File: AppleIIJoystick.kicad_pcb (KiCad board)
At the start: 2 copper layers, 18 parts, among them J1 DB9_Male, J2 Parallax_27800_Joystick, SW1 SW_Push, SW2 SW_Push

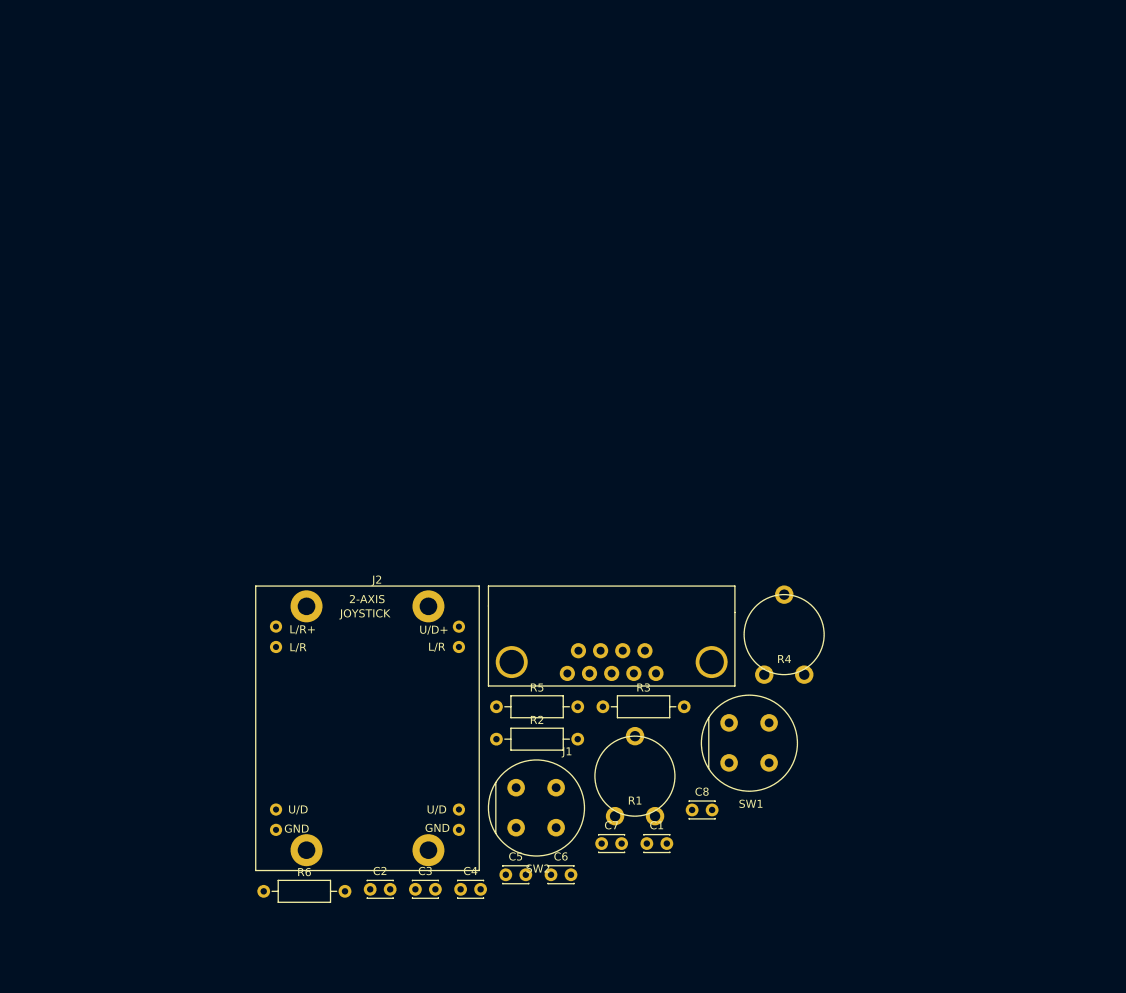
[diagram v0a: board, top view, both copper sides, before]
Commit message: swapped out buttons. new footprint/3d model.
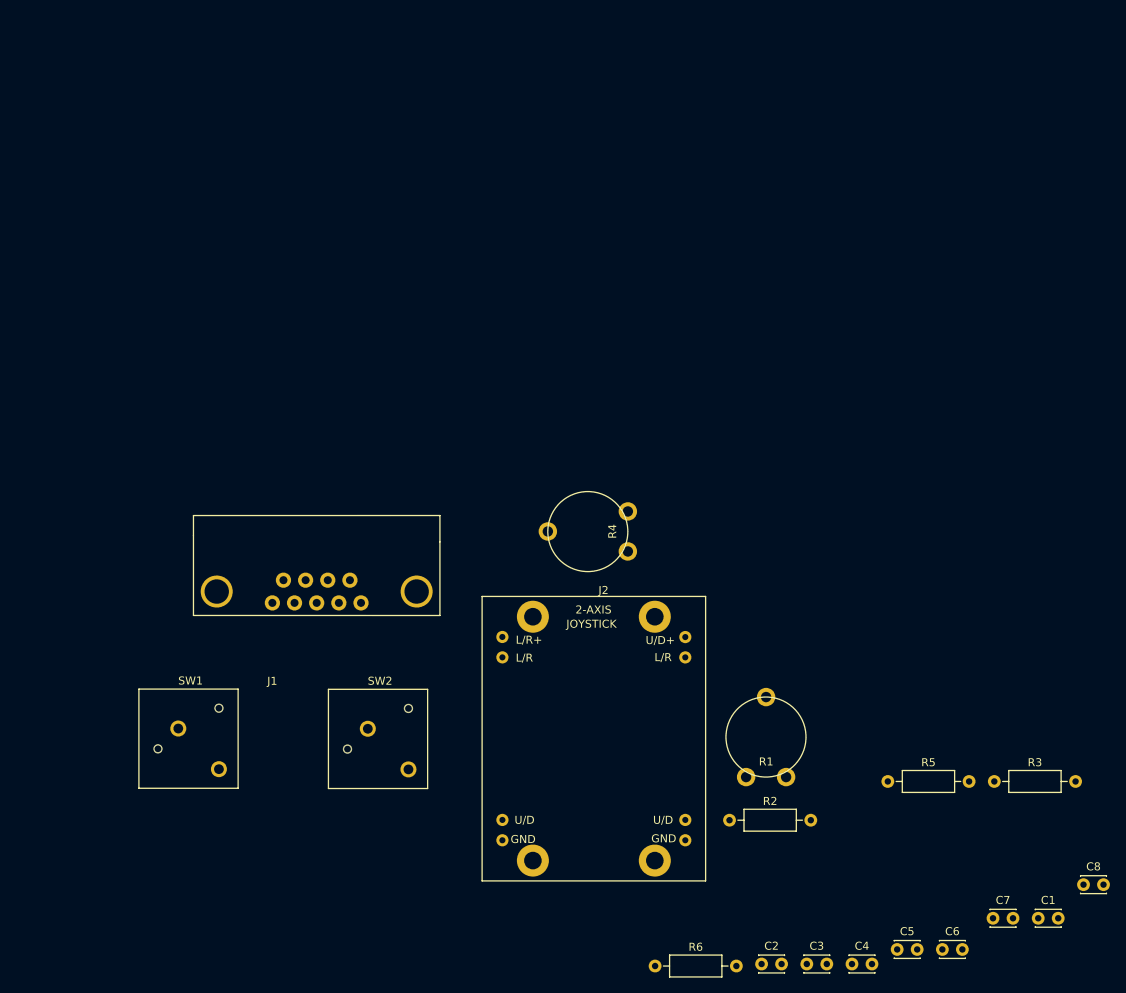
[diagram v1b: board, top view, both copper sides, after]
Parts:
- SW1, SW2: footprint AppleIIJoystick:D6C_BUTTON -> AppleIIJoystick:ESWITCH_E11GRY_BTN
- moved SW1 64.0 mm to (100.8, 134.1)
- moved C1 49.8 mm to (203.2, 152.8)
- moved C4 49.8 mm to (180.0, 158.5)
- moved C5 49.8 mm to (185.6, 156.7)
- moved C7 49.8 mm to (197.6, 152.8)
- moved C8 49.8 mm to (208.9, 148.6)
- moved R3 49.8 mm to (197.8, 135.7)
- moved C2 49.8 mm to (168.7, 158.5)
- moved C3 49.8 mm to (174.3, 158.5)
- moved R6 49.8 mm to (155.4, 158.7)
- moved C6 49.8 mm to (191.3, 156.7)
- moved R5 49.8 mm to (184.4, 135.7)
- moved J1 37.9 mm to (107.5, 113.3)
- moved R2 30.8 mm to (164.7, 140.5)
- moved R4 30.6 mm to (142.0, 104.4), turned to 90 degrees
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
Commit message: adding edge cuts layer and board outline
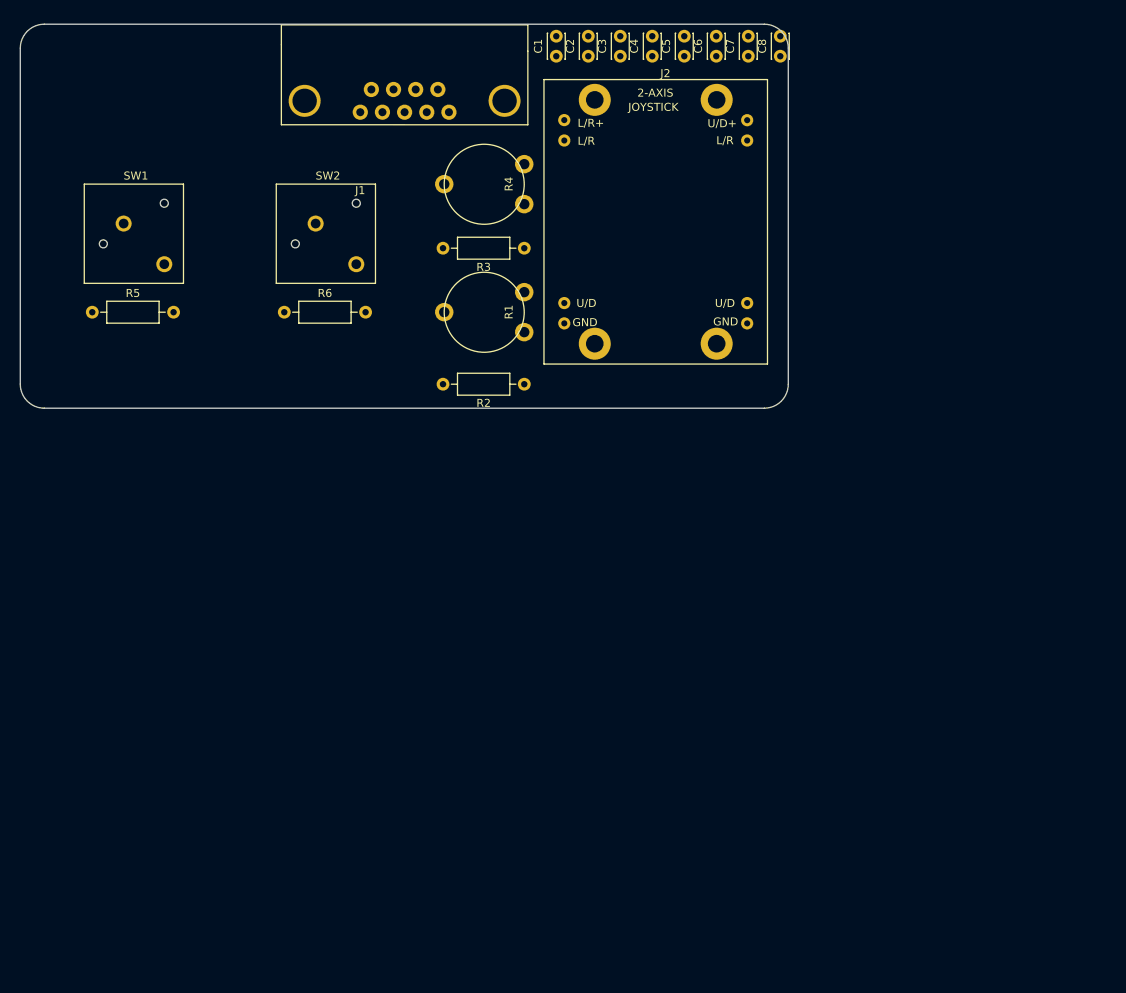
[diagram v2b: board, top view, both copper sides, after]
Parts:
- moved C1 123.5 mm to (143.0, 45.0), turned to 90 degrees
- moved C4 116.2 mm to (155.0, 45.0), turned to 90 degrees
- moved C3 115.8 mm to (151.0, 45.0), turned to 90 degrees
- moved C2 115.5 mm to (147.0, 45.0), turned to 90 degrees
- moved R5 115.5 mm to (85.0, 77.0)
- moved C6 115.2 mm to (163.0, 45.0), turned to 90 degrees
- moved C5 114.8 mm to (159.0, 45.0), turned to 90 degrees
- moved C7 112.0 mm to (167.0, 45.0), turned to 90 degrees
- moved C8 110.3 mm to (171.0, 45.0), turned to 90 degrees
- moved R6 94.0 mm to (109.0, 77.0)
- moved R3 88.9 mm to (139.0, 69.0), turned to 180 degrees
- moved J2 65.1 mm to (144.0, 53.0)
- moved SW1 63.5 mm to (94.0, 71.0)
- moved SW2 63.5 mm to (118.0, 71.0)
- moved R1 62.7 mm to (129.0, 77.0), turned to 90 degrees
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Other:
- board outline added: 96 x 48 mm

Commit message: board layout
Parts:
- moved C4 4.12 mm to (150.9, 44.8)
- moved C8 3.52 mm to (167.5, 44.9)
- moved C3 2.76 mm to (148.2, 44.8)
- moved C7 2.16 mm to (164.8, 44.9)
- moved C2 1.41 mm to (145.6, 44.8)
- moved C6 0.81 mm to (162.2, 44.9)
- moved C5 0.57 mm to (159.6, 44.9)
- moved C1 0.20 mm to (143.0, 44.8)
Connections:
- R1 pad 1: Net-(R1-Pad1) -> /LR
- R1 pad 2: /LR -> Net-(R1-Pad2)
- R2 pad 2: Net-(R1-Pad1) -> Net-(R1-Pad2)
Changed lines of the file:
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@@
   (net 12 "Net-(J2-Pad8)")
   (net 13 "Net-(J2-Pad1)")
-  (net 14 "Net-(R1-Pad1)")
-  (net 15 "Net-(R3-Pad2)")
+  (net 14 "Net-(R3-Pad2)")
+  (net 15 "Net-(R1-Pad2)")
   (net_class Default "This is the default net class."
     (clearance 0.2)
@@
     (add_net "Net-(J2-Pad5)")
     (add_net "Net-(J2-Pad8)")
-    (add_net "Net-(R1-Pad1)")
+    (add_net "Net-(R1-Pad2)")
     (add_net "Net-(R3-Pad2)")
   )
   (module Capacitor_THT:C_Disc_D3.0mm_W2.0mm_P2.50mm (layer F.Cu)
-    (at 143 45 90)
-    (descr "C, Disc series, Radial, pin pitch=2.50mm, , diameter*width=3*2mm^2, Capacitor")
-    (tags "C Disc series Radial pin pitch 2.50mm  diameter 3mm width 2mm Capacitor")
-    (fp_text reference C1 (at 1.25 -2.25 90) (layer F.SilkS)
+    (at 142.96644 44.8056 90)
+    (descr "C, Disc series, Radial, pin pitch=2.50mm, , diameter*width=3*2mm^2, Capacitor")
+    (tags "C Disc series Radial pin pitch 2.50mm  diameter 3mm width 2mm Capacitor")
+    (fp_text reference C1 (at -1.91634 0.03248 90) (layer F.SilkS)
       (effects (font (size 1 1) (thickness 0.15)))
     )
@@
   )
   (module Capacitor_THT:C_Disc_D3.0mm_W2.0mm_P2.50mm (layer F.Cu)
-    (at 147 45 90)
-    (descr "C, Disc series, Radial, pin pitch=2.50mm, , diameter*width=3*2mm^2, Capacitor")
-    (tags "C Disc series Radial pin pitch 2.50mm  diameter 3mm width 2mm Capacitor")
-    (fp_text reference C2 (at 1.25 -2.25 90) (layer F.SilkS)
+    (at 145.6055 44.8056 90)
+    (descr "C, Disc series, Radial, pin pitch=2.50mm, , diameter*width=3*2mm^2, Capacitor")
+    (tags "C Disc series Radial pin pitch 2.50mm  diameter 3mm width 2mm Capacitor")
+    (fp_text reference C2 (at -1.94936 0.0914 90) (layer F.SilkS)
       (effects (font (size 1 1) (thickness 0.15)))
     )
@@
   )
   (module Capacitor_THT:C_Disc_D3.0mm_W2.0mm_P2.50mm (layer F.Cu)
-    (at 151 45 90)
-    (descr "C, Disc series, Radial, pin pitch=2.50mm, , diameter*width=3*2mm^2, Capacitor")
-    (tags "C Disc series Radial pin pitch 2.50mm  diameter 3mm width 2mm Capacitor")
-    (fp_text reference C3 (at 1.25 -2.25 90) (layer F.SilkS)
+    (at 148.24456 44.8056 90)
+    (descr "C, Disc series, Radial, pin pitch=2.50mm, , diameter*width=3*2mm^2, Capacitor")
+    (tags "C Disc series Radial pin pitch 2.50mm  diameter 3mm width 2mm Capacitor")
+    (fp_text reference C3 (at -1.91634 0.04872 90) (layer F.SilkS)
       (effects (font (size 1 1) (thickness 0.15)))
     )
@@
   )
   (module Capacitor_THT:C_Disc_D3.0mm_W2.0mm_P2.50mm (layer F.Cu)
-    (at 155 45 90)
-    (descr "C, Disc series, Radial, pin pitch=2.50mm, , diameter*width=3*2mm^2, Capacitor")
-    (tags "C Disc series Radial pin pitch 2.50mm  diameter 3mm width 2mm Capacitor")
-    (fp_text reference C4 (at 1.25 -2.25 90) (layer F.SilkS)
+    (at 150.88362 44.8056 90)
+    (descr "C, Disc series, Radial, pin pitch=2.50mm, , diameter*width=3*2mm^2, Capacitor")
+    (tags "C Disc series Radial pin pitch 2.50mm  diameter 3mm width 2mm Capacitor")
+    (fp_text reference C4 (at -1.94936 0.00858 90) (layer F.SilkS)
       (effects (font (size 1 1) (thickness 0.15)))
     )
@@
   )
   (module Capacitor_THT:C_Disc_D3.0mm_W2.0mm_P2.50mm (layer F.Cu)
-    (at 159 45 90)
-    (descr "C, Disc series, Radial, pin pitch=2.50mm, , diameter*width=3*2mm^2, Capacitor")
-    (tags "C Disc series Radial pin pitch 2.50mm  diameter 3mm width 2mm Capacitor")
-    (fp_text reference C5 (at 1.25 -2.25 90) (layer F.SilkS)
+    (at 159.56134 44.90094 90)
+    (descr "C, Disc series, Radial, pin pitch=2.50mm, , diameter*width=3*2mm^2, Capacitor")
+    (tags "C Disc series Radial pin pitch 2.50mm  diameter 3mm width 2mm Capacitor")
+    (fp_text reference C5 (at -1.9519 -0.0341 90) (layer F.SilkS)
       (effects (font (size 1 1) (thickness 0.15)))
     )
@@
   )
   (module Capacitor_THT:C_Disc_D3.0mm_W2.0mm_P2.50mm (layer F.Cu)
-    (at 163 45 90)
-    (descr "C, Disc series, Radial, pin pitch=2.50mm, , diameter*width=3*2mm^2, Capacitor")
-    (tags "C Disc series Radial pin pitch 2.50mm  diameter 3mm width 2mm Capacitor")
-    (fp_text reference C6 (at 1.25 -2.25 90) (layer F.SilkS)
+    (at 162.19932 44.90466 90)
+    (descr "C, Disc series, Radial, pin pitch=2.50mm, , diameter*width=3*2mm^2, Capacitor")
+    (tags "C Disc series Radial pin pitch 2.50mm  diameter 3mm width 2mm Capacitor")
+    (fp_text reference C6 (at -1.9519 0.02482 90) (layer F.SilkS)
       (effects (font (size 1 1) (thickness 0.15)))
     )
@@
   )
   (module Capacitor_THT:C_Disc_D3.0mm_W2.0mm_P2.50mm (layer F.Cu)
-    (at 167 45 90)
-    (descr "C, Disc series, Radial, pin pitch=2.50mm, , diameter*width=3*2mm^2, Capacitor")
-    (tags "C Disc series Radial pin pitch 2.50mm  diameter 3mm width 2mm Capacitor")
-    (fp_text reference C7 (at 1.25 -2.25 90) (layer F.SilkS)
+    (at 164.83838 44.90466 90)
+    (descr "C, Disc series, Radial, pin pitch=2.50mm, , diameter*width=3*2mm^2, Capacitor")
+    (tags "C Disc series Radial pin pitch 2.50mm  diameter 3mm width 2mm Capacitor")
+    (fp_text reference C7 (at -1.9519 0.0812 90) (layer F.SilkS)
       (effects (font (size 1 1) (thickness 0.15)))
     )
@@
   )
   (module Capacitor_THT:C_Disc_D3.0mm_W2.0mm_P2.50mm (layer F.Cu)
-    (at 171 45 90)
-    (descr "C, Disc series, Radial, pin pitch=2.50mm, , diameter*width=3*2mm^2, Capacitor")
-    (tags "C Disc series Radial pin pitch 2.50mm  diameter 3mm width 2mm Capacitor")
-    (fp_text reference C8 (at 1.25 -2.25 90) (layer F.SilkS)
+    (at 167.47744 44.90466 90)
+    (descr "C, Disc series, Radial, pin pitch=2.50mm, , diameter*width=3*2mm^2, Capacitor")
+    (tags "C Disc series Radial pin pitch 2.50mm  diameter 3mm width 2mm Capacitor")
+    (fp_text reference C8 (at -1.9519 0.03852 90) (layer F.SilkS)
       (effects (font (size 1 1) (thickness 0.15)))
     )
@@
     (fp_circle (center -0.00762 4.9911) (end 0.01524 9.99236) (layer F.SilkS) (width 0.15))
     (pad 1 thru_hole circle (at 0.00762 -0.00508 90) (size 2.3 2.3) (drill 1.3) (layers *.Cu *.Mask)
-      (net 14 "Net-(R1-Pad1)"))
+      (net 1 /LR))
     (pad 2 thru_hole circle (at 2.50762 9.99492 90) (size 2.3 2.3) (drill 1.3) (layers *.Cu *.Mask)
-      (net 1 /LR))
+      (net 15 "Net-(R1-Pad2)"))
     (pad 3 thru_hole circle (at -2.49238 9.99492 90) (size 2.3 2.3) (drill 1.3) (layers *.Cu *.Mask))
     (model ${KIPRJMOD}/10-PIHER_3D_PT10LV10.STEP
@@
       (net 13 "Net-(J2-Pad1)"))
     (pad 2 thru_hole oval (at 10.16 0 180) (size 1.6 1.6) (drill 0.8) (layers *.Cu *.Mask)
-      (net 14 "Net-(R1-Pad1)"))
+      (net 15 "Net-(R1-Pad2)"))
     (model ${KISYS3DMOD}/Resistor_THT.3dshapes/R_Axial_DIN0207_L6.3mm_D2.5mm_P10.16mm_Horizontal.wrl
       (at (xyz 0 0 0))
@@
     (fp_line (start 1.93 -1.25) (end 1.93 1.25) (layer F.Fab) (width 0.1))
     (pad 2 thru_hole oval (at 10.16 0 180) (size 1.6 1.6) (drill 0.8) (layers *.Cu *.Mask)
-      (net 15 "Net-(R3-Pad2)"))
+      (net 14 "Net-(R3-Pad2)"))
     (pad 1 thru_hole circle (at 0 0 180) (size 1.6 1.6) (drill 0.8) (layers *.Cu *.Mask)
       (net 12 "Net-(J2-Pad8)"))
@@
     (pad 3 thru_hole circle (at -2.49238 9.99492 90) (size 2.3 2.3) (drill 1.3) (layers *.Cu *.Mask))
     (pad 2 thru_hole circle (at 2.50762 9.99492 90) (size 2.3 2.3) (drill 1.3) (layers *.Cu *.Mask)
-      (net 15 "Net-(R3-Pad2)"))
+      (net 14 "Net-(R3-Pad2)"))
     (pad 1 thru_hole circle (at 0.00762 -0.00508 90) (size 2.3 2.3) (drill 1.3) (layers *.Cu *.Mask)
       (net 3 /UD))

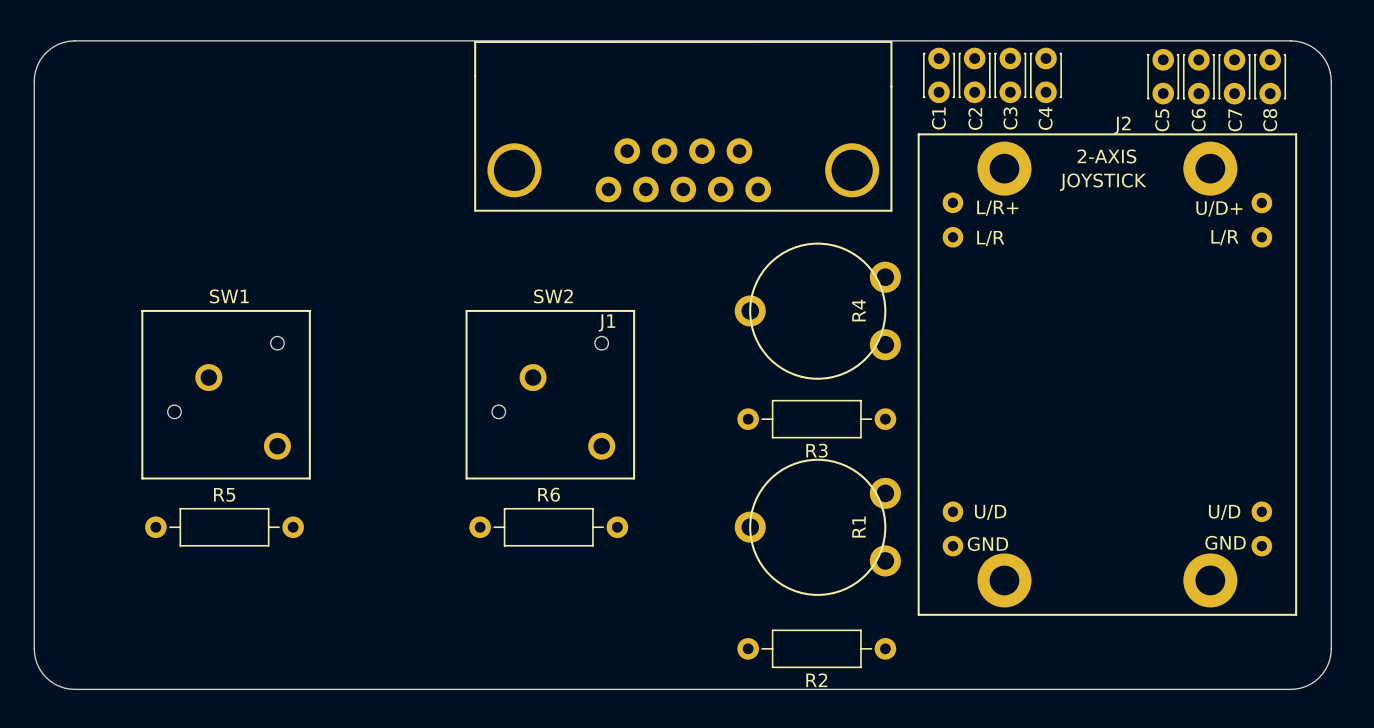
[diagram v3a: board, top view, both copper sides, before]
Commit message: finished routing pcb
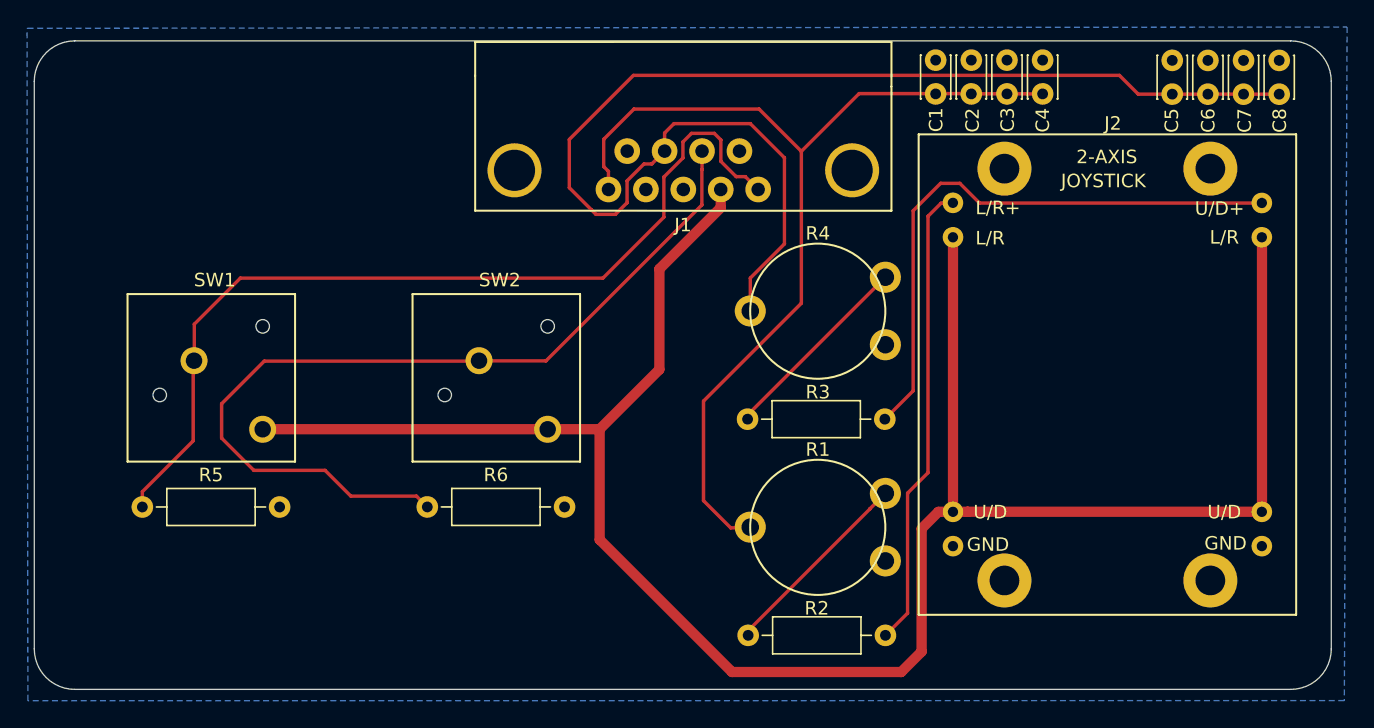
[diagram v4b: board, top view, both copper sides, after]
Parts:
- moved SW2 4.19 mm to (114.0, 69.8)
- moved R6 4.19 mm to (105.1, 75.5)
- moved R5 1.80 mm to (84.0, 75.5)
- moved SW1 1.66 mm to (92.9, 69.8)
- moved R2 1.00 mm to (139.0, 85.0)
- moved C5 0.67 mm to (160.2, 44.9)
- moved C6 0.67 mm to (162.9, 44.9)
- moved C7 0.67 mm to (165.5, 44.9)
- moved C8 0.67 mm to (168.1, 44.9)
- moved C1 0.28 mm to (142.7, 44.9)
- moved C2 0.28 mm to (145.4, 44.9)
- moved C3 0.28 mm to (148.0, 44.9)
- moved C4 0.28 mm to (150.6, 44.9)
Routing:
- net /+5V: track 0.00 -> 158.6 mm
- net /UD: track 0.00 -> 93.6 mm
- net /LR: track 0.00 -> 73.4 mm
- net /PB1: track 0.00 -> 67.8 mm
- net /PB0: track 0.00 -> 65.6 mm
- net Net-(J2-Pad8): track 0.00 -> 43.5 mm
- net Net-(J2-Pad1): track 0.00 -> 34.6 mm
- net Net-(R1-Pad2): track 0.00 -> 14.8 mm
- net Net-(R3-Pad2): track 0.00 -> 14.7 mm
- added copper zone on B.Cu, net GND

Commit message: added gerber
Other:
- board text added: "APPLE ][ JOYSTICK"
